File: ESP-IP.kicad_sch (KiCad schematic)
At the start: 32 parts, among them J1 Serial and power, J2 Programming Pads, Q1 L78M05ABDT-TR, SW1 SW_Push, SW2 SW_Push, U1 ESP32-WROOM-32U, U3 TXS0102DCU, U4 AMS1117-3.3

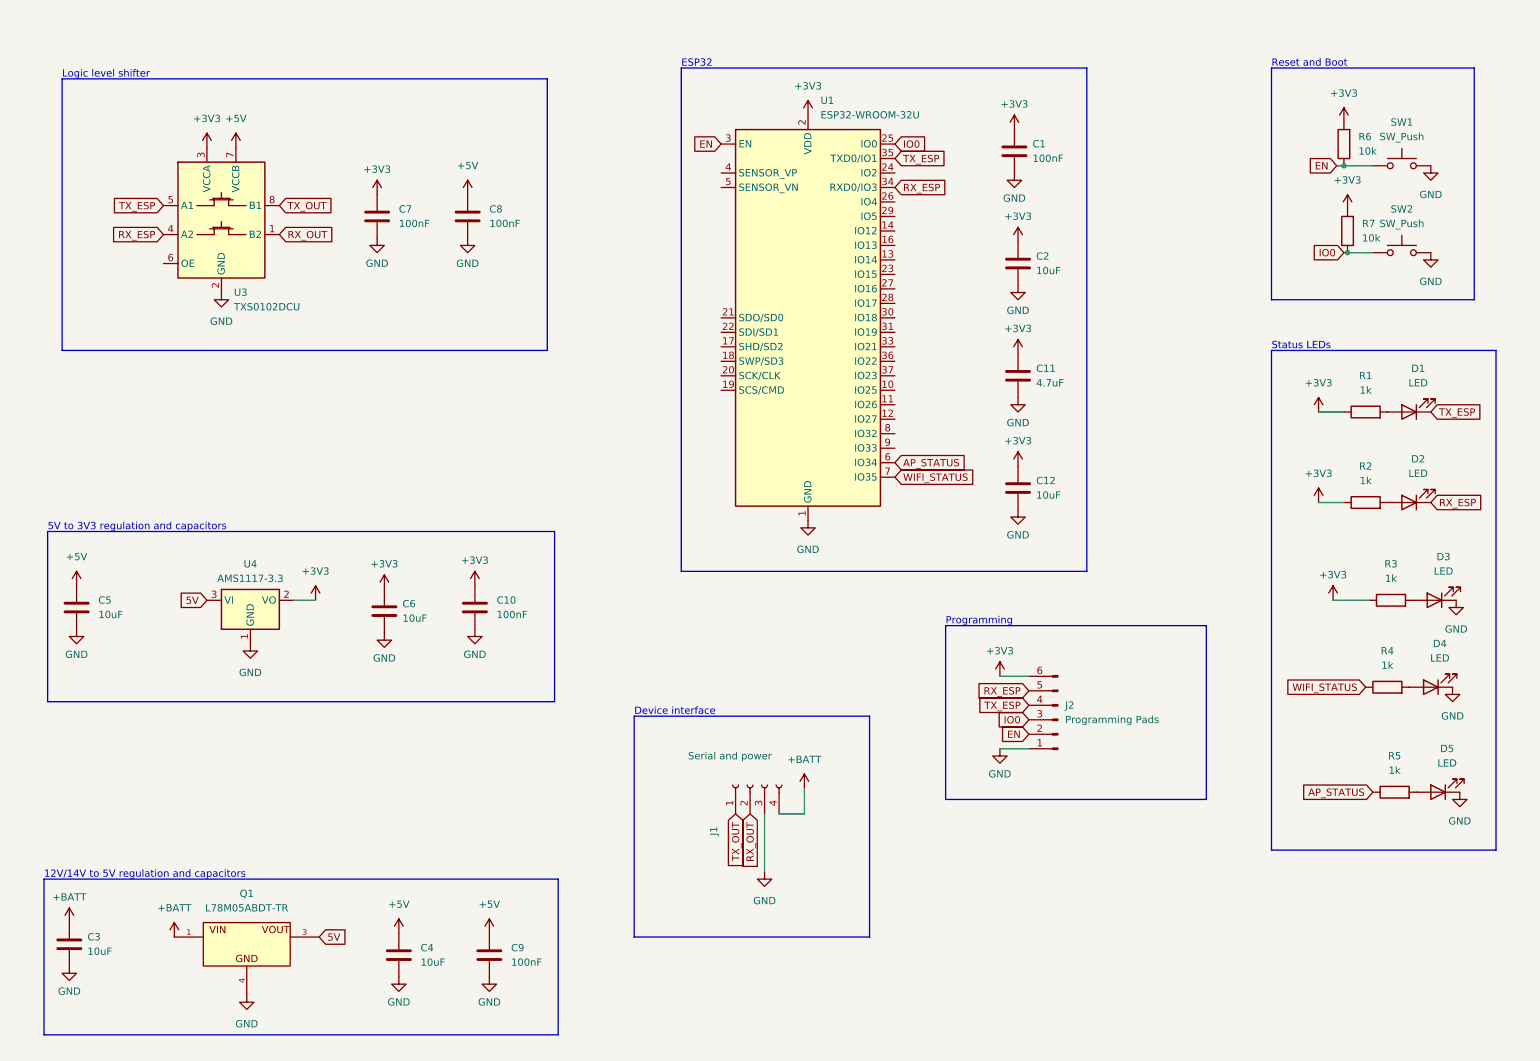
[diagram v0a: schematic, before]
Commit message: my suggested board layout, includes schematic fixes, part number allocation and PCB, routing TBD
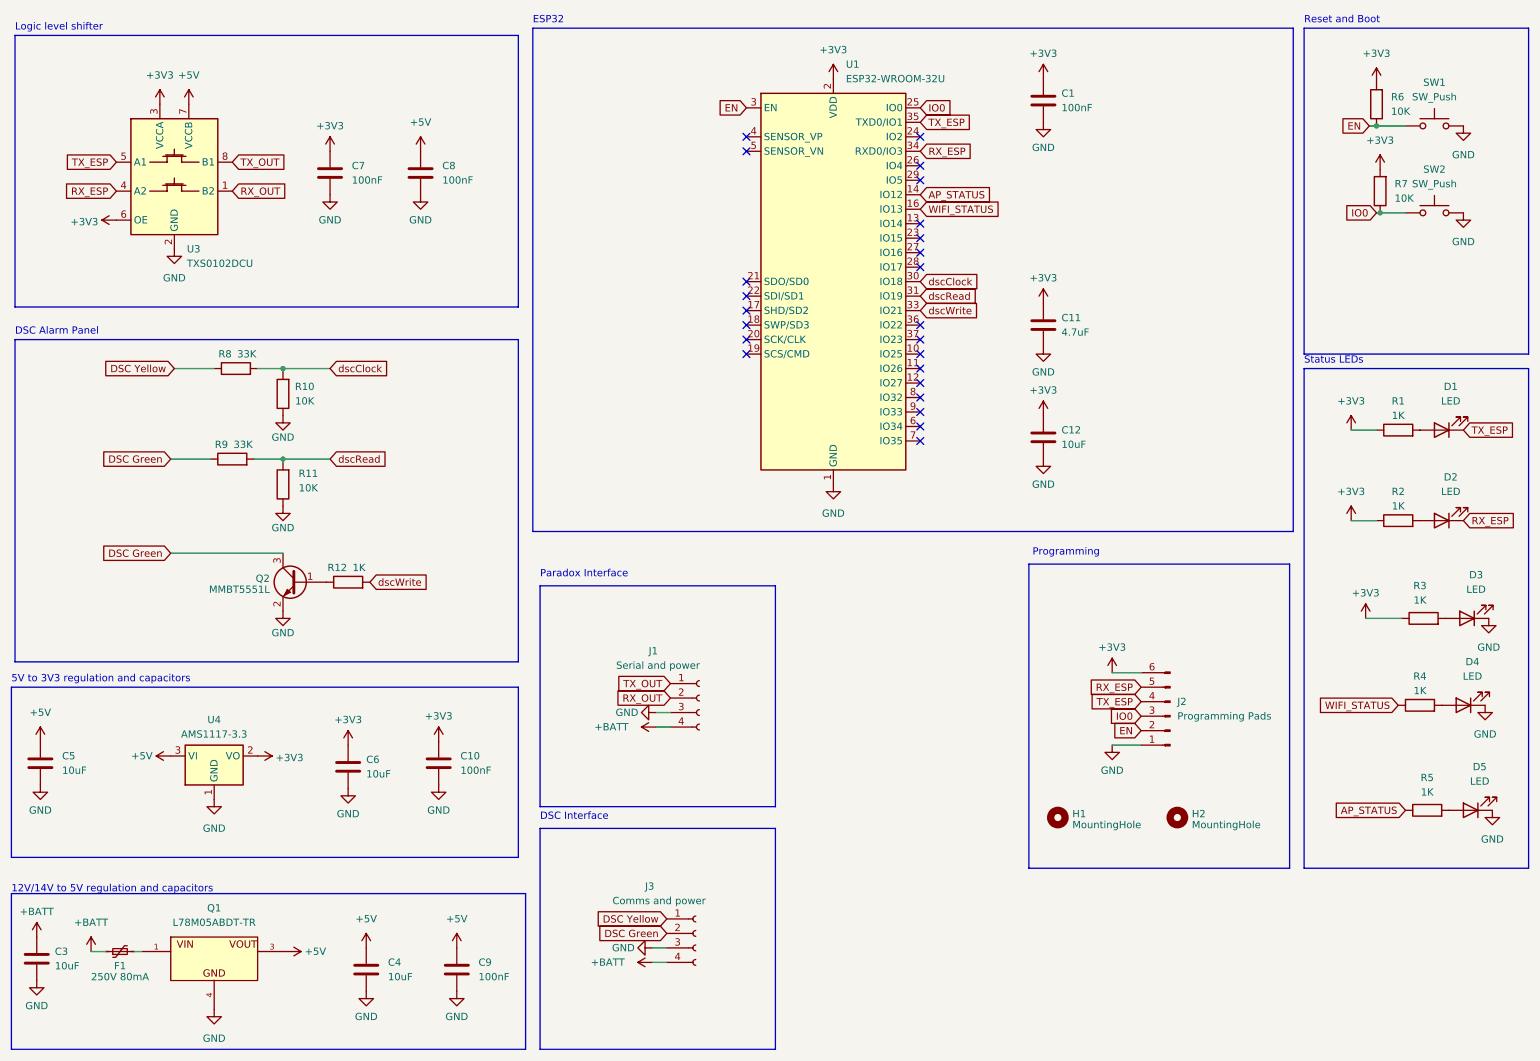
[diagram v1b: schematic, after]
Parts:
- removed C2: 10uF, Capacitor_SMD:C_0805_2012Metric, symbol Device:C
- added F1: 250V 80mA, Fuse:Fuse_Bourns_MF-RG300, symbol Device:Polyfuse_Small
- added H1, H2: MountingHole, MountingHole:MountingHole_2.7mm_M2.5, symbol Mechanical:MountingHole
- added J3: Comms and power, Connector_PinHeader_2.54mm:PinHeader_1x04_P2.54mm_Horizontal, symbol Connector:Conn_01x04_Socket
- added Q2: MMBT5551L, Package_TO_SOT_SMD:SOT-23, symbol Transistor_BJT:MMBT5551L
- added R10, R11: 10K, Resistor_SMD:R_0402_1005Metric, symbol Device:R
- added R12: 1K, Resistor_SMD:R_0402_1005Metric, symbol Device:R
- added R8, R9: 33K, Resistor_SMD:R_0402_1005Metric, symbol Device:R
- C1, C10, C7, C8, C9: footprint Capacitor_SMD:C_0805_2012Metric -> Capacitor_SMD:C_0402_1005Metric; LCSC (none) -> C307331
- C11: footprint Capacitor_SMD:C_0805_2012Metric -> Capacitor_SMD:C_0402_1005Metric; LCSC (none) -> C1538
- C12, C3, C4, C5, C6: footprint Capacitor_SMD:C_0805_2012Metric -> Capacitor_SMD:C_0603_1608Metric; LCSC (none) -> C57112
- D1, D2: footprint LED_SMD:LED_0805_2012Metric -> LED_SMD:LED_0603_1608Metric; LCSC (none) -> C2286
- D3: footprint LED_SMD:LED_0805_2012Metric -> LED_SMD:LED_0603_1608Metric; LCSC (none) -> C72038
- D4: footprint LED_SMD:LED_0805_2012Metric -> LED_SMD:LED_0603_1608Metric; LCSC (none) -> C72041
- D5: footprint LED_SMD:LED_0805_2012Metric -> LED_SMD:LED_0603_1608Metric; LCSC (none) -> C72043
- J1: footprint Connector_PinSocket_2.54mm:PinSocket_1x04_P2.54mm_Vertical -> Connector_PinHeader_2.54mm:PinHeader_1x04_P2.54mm_Horizontal; LCSC (none) -> DNP; MicroRobotics (none) -> https://www.robotics.org.za/TC-4P-254?search=terminal
- J2: footprint Connector_PinHeader_1.27mm:PinHeader_1x06_P1.27mm_Vertical -> Connector_PinHeader_2.54mm:PinHeader_1x06_P2.54mm_Vertical_SMD_Pin1Left; LCSC (none) -> DNP
- R1: value 1k -> 1K; footprint LED_SMD:LED_0402_1005Metric -> Resistor_SMD:R_0402_1005Metric; LCSC (none) -> C11702
- R2, R3, R4, R5: value 1k -> 1K; footprint Resistor_SMD:R_0805_2012Metric -> Resistor_SMD:R_0402_1005Metric; LCSC (none) -> C11702
- R6, R7: value 10k -> 10K; footprint Resistor_SMD:R_0805_2012Metric -> Resistor_SMD:R_0402_1005Metric; LCSC (none) -> C25744
- SW1, SW2: JLC C318884 -> (none); LCSC (none) -> C318884
- U1: LCSC (none) -> DNP; MicroRobotics (none) -> ESP32 WROOM 32UE
- U3: JLC C53434 -> (none); LCSC (none) -> C53434
- U4: LCSC (none) -> C6186
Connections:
- net 5V is gone; now on net +5V: Q1.3 (OUT), U4.3 (VI)
- net +3V3: now also U3.6 (OE)
- net +BATT: now also F1.1, J3.4 (Pin_4); no longer Q1.1 (IN)
- net AP_STATUS: now also U1.14 (IO12); no longer U1.6 (IO34)
- net GND: now also J3.3 (Pin_3), Q2.2 (E), R10.1, R11.1
- net WIFI_STATUS: now also U1.16 (IO13); no longer U1.7 (IO35)
- net dscClock: now reaches U1.30 (IO18)
- net dscClock: now also R10.2, R8.2
- net dscRead: now reaches U1.31 (IO19)
- net dscRead: now also R11.2, R9.2
- net dscWrite: now reaches U1.33 (IO21)
- net dscWrite: now also R12.2
- new net: F1.2, Q1.1 (IN)
- new net: Q2.1 (B), R12.1
- new net DSC Green: J3.2 (Pin_2), Q2.3 (C), R9.1
- new net DSC Yellow: J3.1 (Pin_1), R8.1
- no-connect marks 0 -> 24
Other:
- note added: "DSC Alarm Panel"
- note added: "DSC Interface"
- note added: "Paradox Interface"
- note removed: "Device interface"
- company: (none) -> Heems
- title: (none) -> Alarm Gateway
- moved on the sheet: C1, C10, C11, C12, C3, C4, C5, C6, C7, C8, C9, D1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

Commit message: chore: switch header back for serial and standardise labels
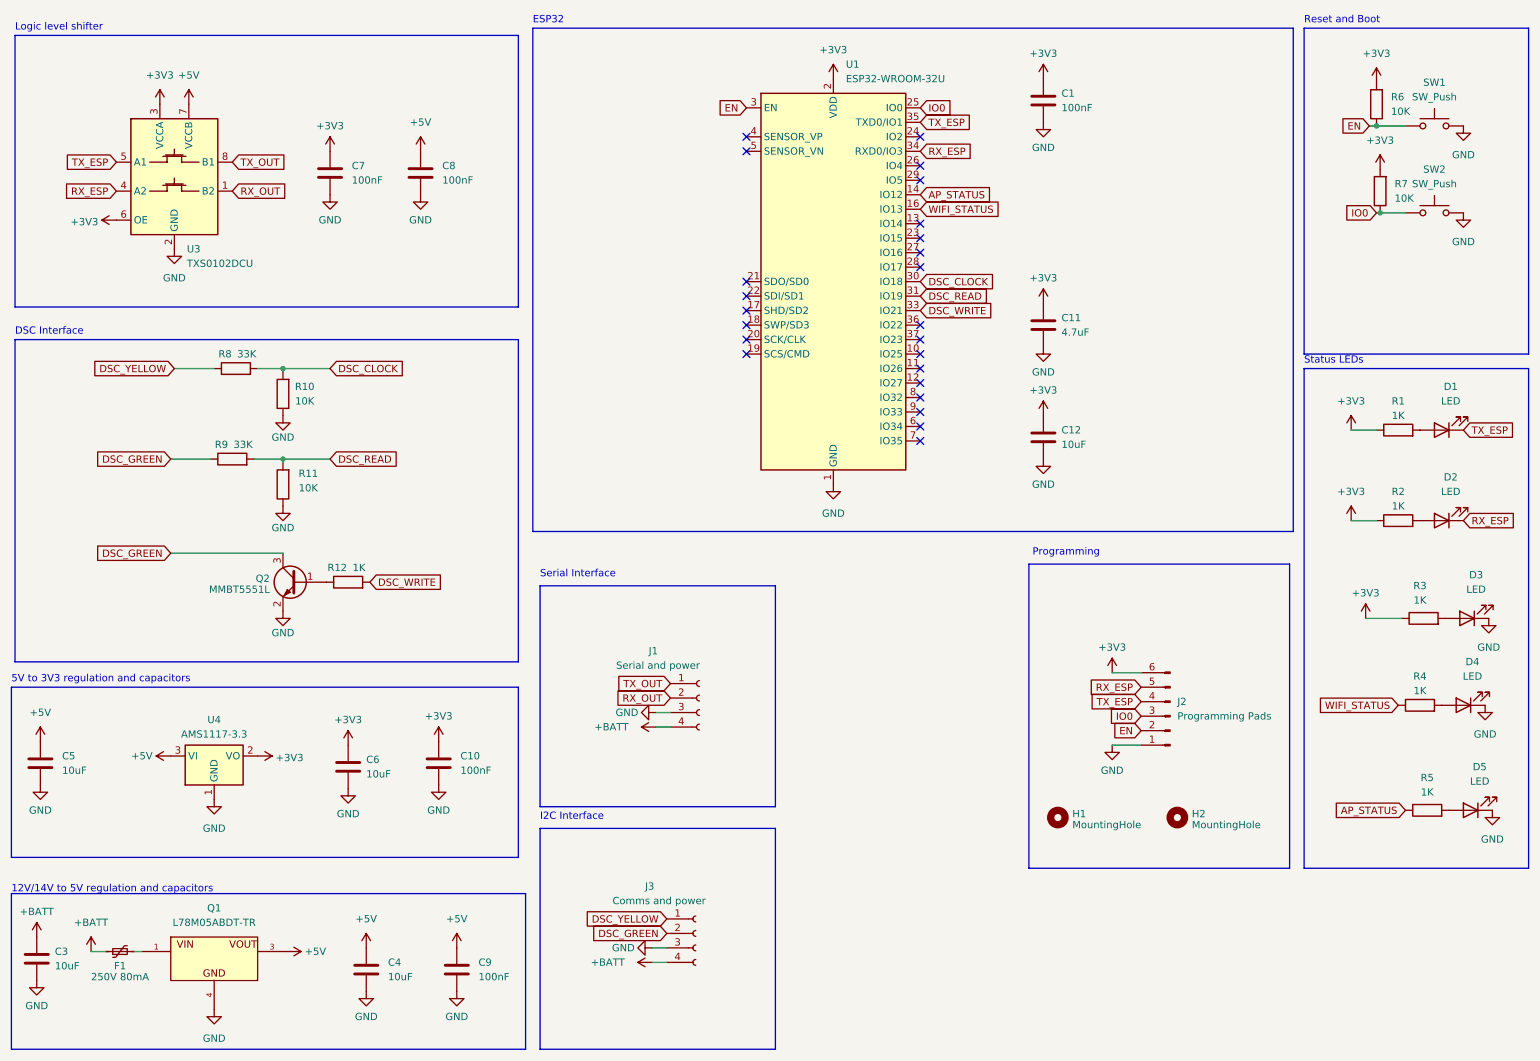
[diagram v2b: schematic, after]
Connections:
- net DSC Green renamed DSC_GREEN
- net DSC Yellow renamed DSC_YELLOW
- net dscClock renamed DSC_CLOCK
- net dscRead renamed DSC_READ
- net dscWrite renamed DSC_WRITE
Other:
- note added: "I2C Interface"
- note added: "Serial Interface"
- note removed: "DSC Alarm Panel"
- note removed: "Paradox Interface"
- title: Alarm Gateway -> ESP32 IP Relay
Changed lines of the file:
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@@
   (paper "A4")
   (title_block
-    (title "Alarm Gateway")
+    (title "ESP32 IP Relay")
     (date "2023-09-25")
     (rev "1.0")
@@
     (effects (font (size 1.27 1.27)) (justify left bottom))
   )
-  (text "DSC Interface\n" (at 108.585 154.305 0)
+  (text "I2C Interface\n" (at 108.585 154.305 0)
     (effects (font (size 1.27 1.27)) (justify left bottom))
   )
@@
     (effects (font (size 1.27 1.27)) (justify left bottom))
   )
-  (text "DSC Alarm Panel" (at 16.51 69.215 0)
+  (text "DSC Interface" (at 16.51 69.215 0)
     (effects (font (size 1.27 1.27)) (justify left bottom))
   )
@@
     (effects (font (size 1.27 1.27)) (justify left bottom))
   )
-  (text "Paradox Interface\n" (at 108.585 111.76 0)
+  (text "Serial Interface\n" (at 108.585 111.76 0)
     (effects (font (size 1.27 1.27)) (justify left bottom))
   )
@@
     )
   )
-  (global_label "DSC Green" (shape input) (at 130.81 173.99 180) (fields_autoplaced)
-    (effects (font (size 1.27 1.27)) (justify right))
-    (property "Intersheetrefs" "${INTERSHEET_REFS}" (at 117.8047 173.99 0)
+  (global_label "DSC_GREEN" (shape input) (at 130.81 173.99 180) (fields_autoplaced)
+    (effects (font (size 1.27 1.27)) (justify right))
+    (property "Intersheetrefs" "${INTERSHEET_REFS}" (at 116.9392 173.99 0)
       (effects (font (size 1.27 1.27)) (justify right) hide)
     )
@@
     )
   )
-  (global_label "dscRead" (shape input) (at 175.26 62.23 0) (fields_autoplaced)
-    (effects (font (size 1.27 1.27)) (justify left))
-    (property "Intersheetrefs" "${INTERSHEET_REFS}" (at 186.0881 62.23 0)
-      (effects (font (size 1.27 1.27)) (justify left) hide)
-    )
-  )
-  (global_label "DSC Green" (shape input) (at 43.815 90.805 180) (fields_autoplaced)
-    (effects (font (size 1.27 1.27)) (justify right))
-    (property "Intersheetrefs" "${INTERSHEET_REFS}" (at 30.8097 90.805 0)
+  (global_label "DSC_READ" (shape input) (at 175.26 62.23 0) (fields_autoplaced)
+    (effects (font (size 1.27 1.27)) (justify left))
+    (property "Intersheetrefs" "${INTERSHEET_REFS}" (at 187.7399 62.23 0)
+      (effects (font (size 1.27 1.27)) (justify left) hide)
+    )
+  )
+  (global_label "DSC_GREEN" (shape input) (at 43.815 90.805 180) (fields_autoplaced)
+    (effects (font (size 1.27 1.27)) (justify right))
+    (property "Intersheetrefs" "${INTERSHEET_REFS}" (at 29.9442 90.805 0)
       (effects (font (size 1.27 1.27)) (justify right) hide)
     )
@@
     )
   )
-  (global_label "dscClock" (shape input) (at 71.755 74.93 0) (fields_autoplaced)
-    (effects (font (size 1.27 1.27)) (justify left))
-    (property "Intersheetrefs" "${INTERSHEET_REFS}" (at 83.1274 74.93 0)
+  (global_label "DSC_CLOCK" (shape input) (at 71.755 74.93 0) (fields_autoplaced)
+    (effects (font (size 1.27 1.27)) (justify left))
+    (property "Intersheetrefs" "${INTERSHEET_REFS}" (at 85.6259 74.93 0)
       (effects (font (size 1.27 1.27)) (justify left) hide)
     )
@@
     )
   )
-  (global_label "DSC Yellow" (shape input) (at 130.81 171.45 180) (fields_autoplaced)
-    (effects (font (size 1.27 1.27)) (justify right))
-    (property "Intersheetrefs" "${INTERSHEET_REFS}" (at 117.2 171.45 0)
+  (global_label "DSC_YELLOW" (shape input) (at 130.81 171.45 180) (fields_autoplaced)
+    (effects (font (size 1.27 1.27)) (justify right))
+    (property "Intersheetrefs" "${INTERSHEET_REFS}" (at 116.032 171.45 0)
       (effects (font (size 1.27 1.27)) (justify right) hide)
     )
@@
     )
   )
-  (global_label "DSC Green" (shape input) (at 43.815 107.315 180) (fields_autoplaced)
-    (effects (font (size 1.27 1.27)) (justify right))
-    (property "Intersheetrefs" "${INTERSHEET_REFS}" (at 30.8097 107.315 0)
+  (global_label "DSC_GREEN" (shape input) (at 43.815 107.315 180) (fields_autoplaced)
+    (effects (font (size 1.27 1.27)) (justify right))
+    (property "Intersheetrefs" "${INTERSHEET_REFS}" (at 29.9442 107.315 0)
       (effects (font (size 1.27 1.27)) (justify right) hide)
     )
@@
     )
   )
-  (global_label "dscWrite" (shape input) (at 175.26 64.77 0) (fields_autoplaced)
-    (effects (font (size 1.27 1.27)) (justify left))
-    (property "Intersheetrefs" "${INTERSHEET_REFS}" (at 186.0882 64.77 0)
+  (global_label "DSC_WRITE" (shape input) (at 175.26 64.77 0) (fields_autoplaced)
+    (effects (font (size 1.27 1.27)) (justify left))
+    (property "Intersheetrefs" "${INTERSHEET_REFS}" (at 188.4051 64.77 0)
       (effects (font (size 1.27 1.27)) (justify left) hide)
     )
@@
     )
   )
-  (global_label "dscRead" (shape input) (at 71.755 90.805 0) (fields_autoplaced)
-    (effects (font (size 1.27 1.27)) (justify left))
-    (property "Intersheetrefs" "${INTERSHEET_REFS}" (at 82.5831 90.805 0)
+  (global_label "DSC_READ" (shape input) (at 71.755 90.805 0) (fields_autoplaced)
+    (effects (font (size 1.27 1.27)) (justify left))
+    (property "Intersheetrefs" "${INTERSHEET_REFS}" (at 84.2349 90.805 0)
       (effects (font (size 1.27 1.27)) (justify left) hide)
     )
@@
     )
   )
-  (global_label "dscWrite" (shape input) (at 78.74 112.395 0) (fields_autoplaced)
-    (effects (font (size 1.27 1.27)) (justify left))
-    (property "Intersheetrefs" "${INTERSHEET_REFS}" (at 89.5682 112.395 0)
+  (global_label "DSC_WRITE" (shape input) (at 78.74 112.395 0) (fields_autoplaced)
+    (effects (font (size 1.27 1.27)) (justify left))
+    (property "Intersheetrefs" "${INTERSHEET_REFS}" (at 91.8851 112.395 0)
       (effects (font (size 1.27 1.27)) (justify left) hide)
     )
@@
     )
   )
-  (global_label "DSC Yellow" (shape input) (at 44.45 74.93 180) (fields_autoplaced)
-    (effects (font (size 1.27 1.27)) (justify right))
-    (property "Intersheetrefs" "${INTERSHEET_REFS}" (at 30.84 74.93 0)
-      (effects (font (size 1.27 1.27)) (justify right) hide)
-    )
-  )
-  (global_label "dscClock" (shape input) (at 175.26 59.69 0) (fields_autoplaced)
-    (effects (font (size 1.27 1.27)) (justify left))
-    (property "Intersheetrefs" "${INTERSHEET_REFS}" (at 186.6324 59.69 0)
-      (effects (font (size 1.27 1.27)) (justify left) hide)
-    )
+  (global_label "DSC_YELLOW" (shape input) (at 44.45 74.93 180) (fields_autoplaced)
+    (effects (font (size 1.27 1.27)) (justify right))
+    (property "Intersheetrefs" "${INTERSHEET_REFS}" (at 29.672 74.93 0)
+      (effects (font (size 1.27 1.27)) (justify right) hide)
+    )
+  )
+  (global_label "DSC_CLOCK" (shape input) (at 175.26 59.69 0) (fields_autoplaced)
+    (effects (font (size 1.27 1.27)) (justify left))
+    (property "Intersheetrefs" "${INTERSHEET_REFS}" (at 189.1309 59.69 0)
+      (effects (font (size 1.27 1.27)) (justify left) hide)
+    )

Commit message: chore: switch back to socket for serial
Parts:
- J1: footprint Connector_PinHeader_2.54mm:PinHeader_1x04_P2.54mm_Horizontal -> Connector_PinSocket_2.54mm:PinSocket_1x04_P2.54mm_Vertical
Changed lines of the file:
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@@
       (effects (font (size 1.27 1.27)) (justify left))
     )
-    (property "Footprint" "Connector_PinHeader_2.54mm:PinHeader_1x04_P2.54mm_Horizontal" (at 136.525 132.715 0)
+    (property "Footprint" "Connector_PinSocket_2.54mm:PinSocket_1x04_P2.54mm_Vertical" (at 136.525 132.715 0)
       (effects (font (size 1.27 1.27)) hide)
     )

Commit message: chore: initial routing
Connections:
- net WIFI_STATUS: now also U1.11 (IO26); no longer U1.16 (IO13)
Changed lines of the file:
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@@
   (no_connect (at 144.78 64.77))
   (no_connect (at 175.26 69.85))
-  (no_connect (at 175.26 74.93))
   (no_connect (at 175.26 77.47))
   (no_connect (at 175.26 57.15))
@@
   (no_connect (at 144.78 69.85))
   (no_connect (at 175.26 82.55))
+  (no_connect (at 175.26 46.99))
   (no_connect (at 175.26 85.09))
   (no_connect (at 144.78 36.83))
@@
     )
   )
-  (global_label "WIFI_STATUS" (shape input) (at 175.26 46.99 0) (fields_autoplaced)
-    (effects (font (size 1.27 1.27)) (justify left))
-    (property "Intersheetrefs" "${INTERSHEET_REFS}" (at 189.7357 46.99 0)
-      (effects (font (size 1.27 1.27)) (justify left) hide)
-    )
-  )
   (global_label "AP_STATUS" (shape input) (at 260.35 152.4 180) (fields_autoplaced)
     (effects (font (size 1.27 1.27)) (justify right))
@@
     )
   )
+  (global_label "WIFI_STATUS" (shape input) (at 175.26 74.93 0) (fields_autoplaced)
+    (effects (font (size 1.27 1.27)) (justify left))
+    (property "Intersheetrefs" "${INTERSHEET_REFS}" (at 189.7357 74.93 0)
+      (effects (font (size 1.27 1.27)) (justify left) hide)
+    )
+  )
